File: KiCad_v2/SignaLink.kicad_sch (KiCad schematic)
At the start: 19 parts, among them U2 ESP32-C3_SUPERMINI_TH, U3 DM-OLED096-636, U7 LTC4415IMSE_PBF

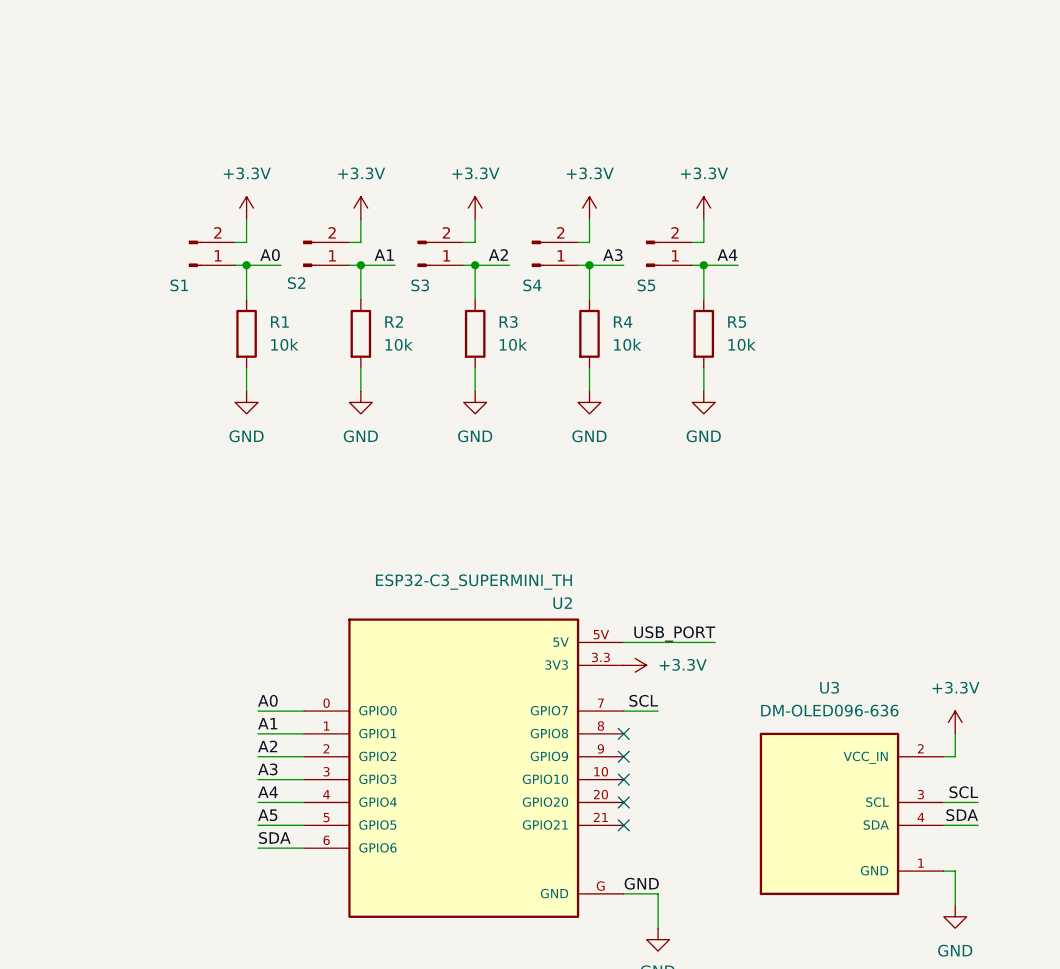
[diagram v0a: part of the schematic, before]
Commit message: feat: agrego 3d de ESP32 Y CM4
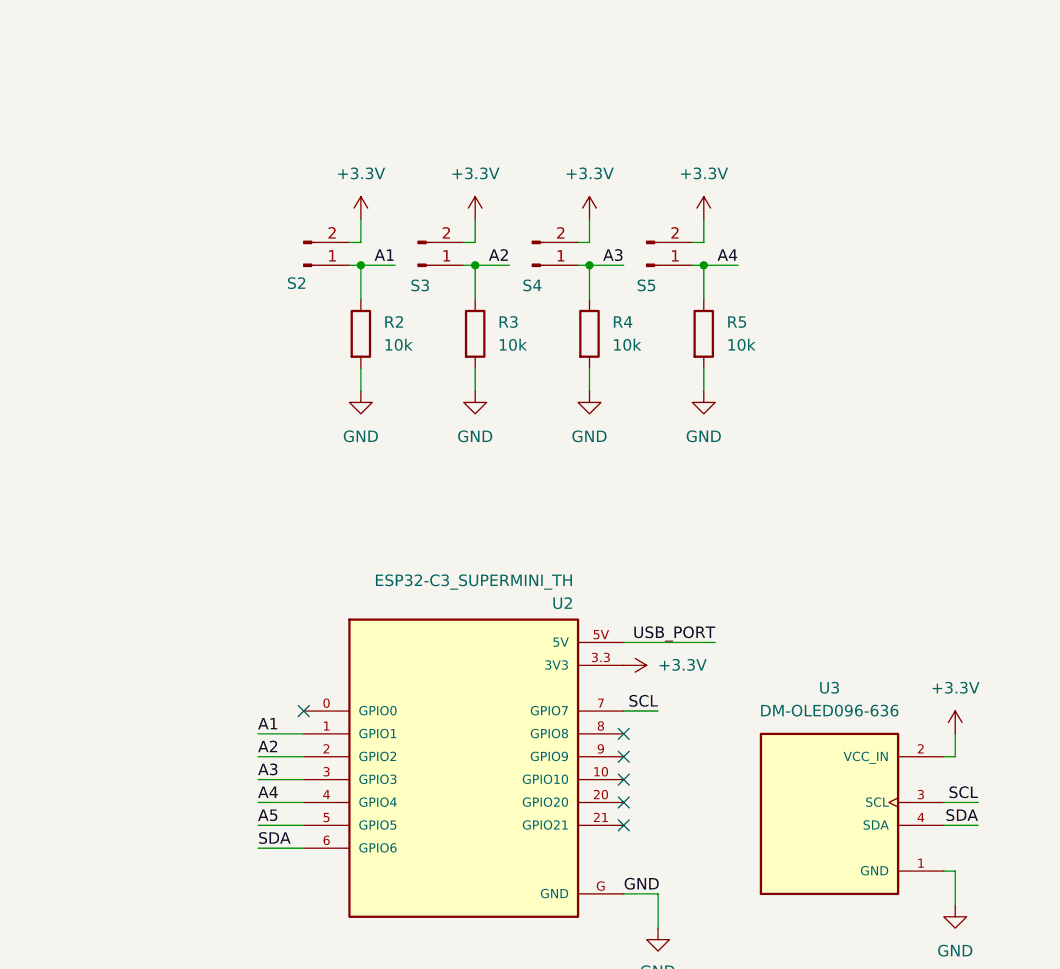
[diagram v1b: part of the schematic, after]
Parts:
- removed R1: 10k, Resistor_SMD:R_0805_2012Metric, symbol Device:R
- removed S1: SF 1, Connector_PinHeader_2.54mm:PinHeader_1x02_P2.54mm_Vertical, symbol Connector:Conn_01x02_Pin
- S2: footprint Connector_PinHeader_2.54mm:PinHeader_1x02_P2.54mm_Vertical -> Molex_KK-254_AE-6410-02A_1x02_P2.54mm_Vertical
- S3, S4: footprint Connector_PinHeader_2.54mm:PinHeader_1x02_P2.54mm_Vertical -> Connector_Molex:Molex_KK-254_AE-6410-02A_1x02_P2.54mm_Vertical
- U2: footprint esp32-huella:MODULE_ESP32-C3_SUPERMINI_TH -> Custom_Footprints:MODULE_ESP32-C3_SUPERMINI_TH
- U3: footprint Connector_PinHeader_2.54mm:PinHeader_1x04_P2.54mm_Vertical -> Custom_Footprints:MODULE_DM-OLED096-636
- U7: footprint Footprint KiCad:MSOP-16_MSE -> Custom_Footprints:MSOP-16_MSE
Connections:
- net A0: no longer names the net of U2.0 (GPIO0)
- no-connect marks 12 -> 13

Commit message: docs: muevo a carpetas los simbolos
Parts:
- S2: footprint Molex_KK-254_AE-6410-02A_1x02_P2.54mm_Vertical -> Connector_Molex:Molex_KK-254_AE-6410-02A_1x02_P2.54mm_Vertical
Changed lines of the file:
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@@
 			)
 		)
-		(property "Footprint" "Molex_KK-254_AE-6410-02A_1x02_P2.54mm_Vertical"
+		(property "Footprint" "Connector_Molex:Molex_KK-254_AE-6410-02A_1x02_P2.54mm_Vertical"
 			(at 52.07 38.1 0)
 			(effects

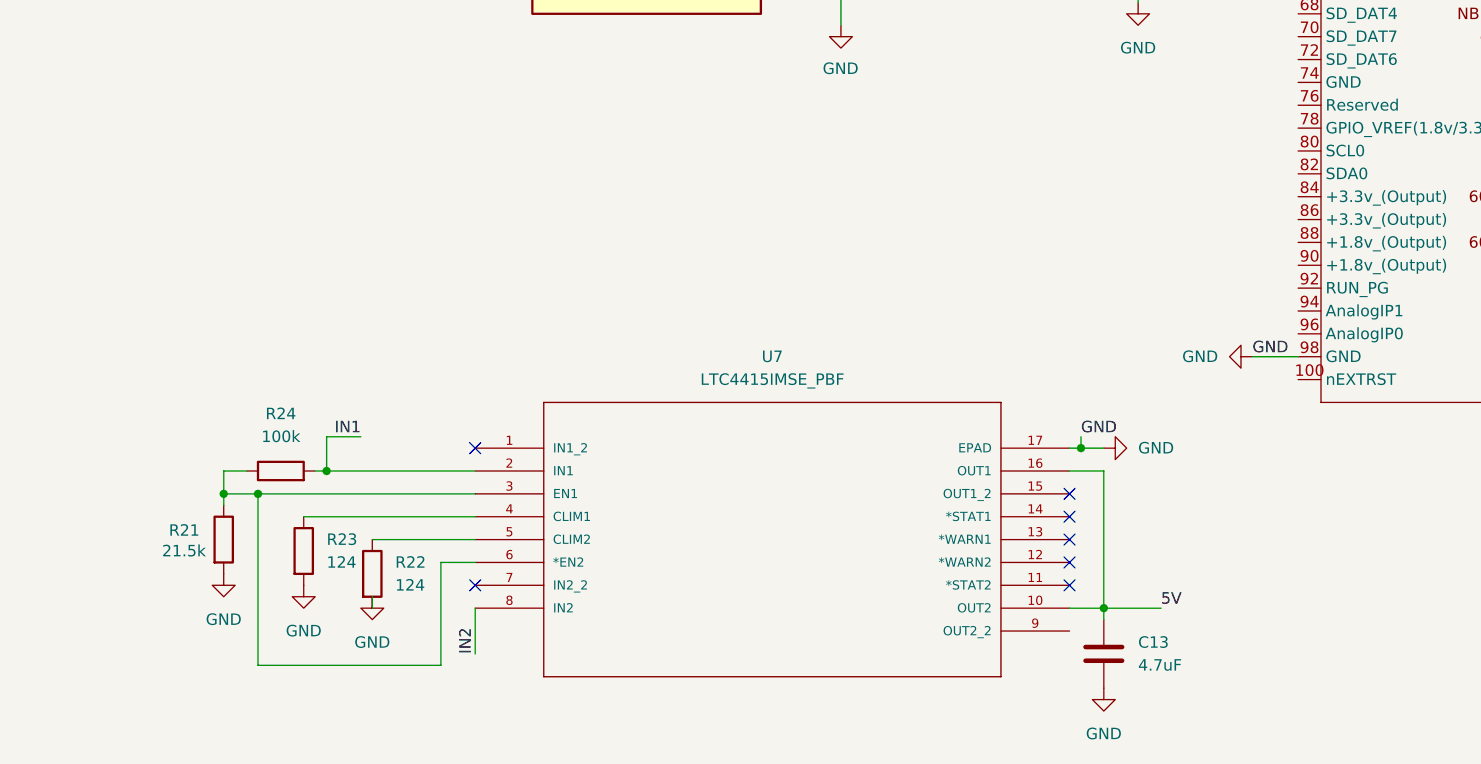
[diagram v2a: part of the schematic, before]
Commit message: agrego step up para 3A con su debido esquematico
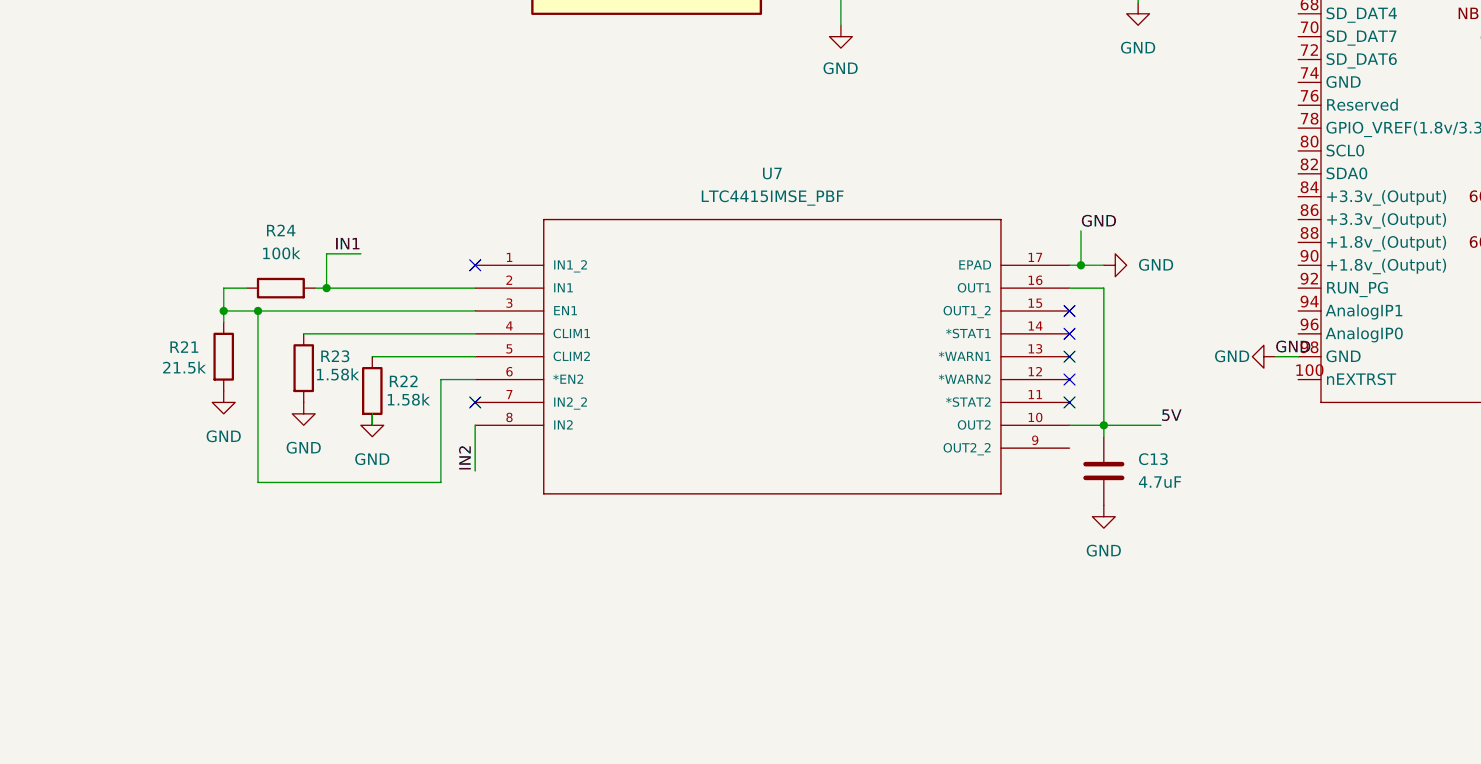
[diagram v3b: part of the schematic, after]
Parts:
- R22, R23: value 124 -> 1.58k
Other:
- moved on the sheet: C13, R21, R22, R23, R24, U7

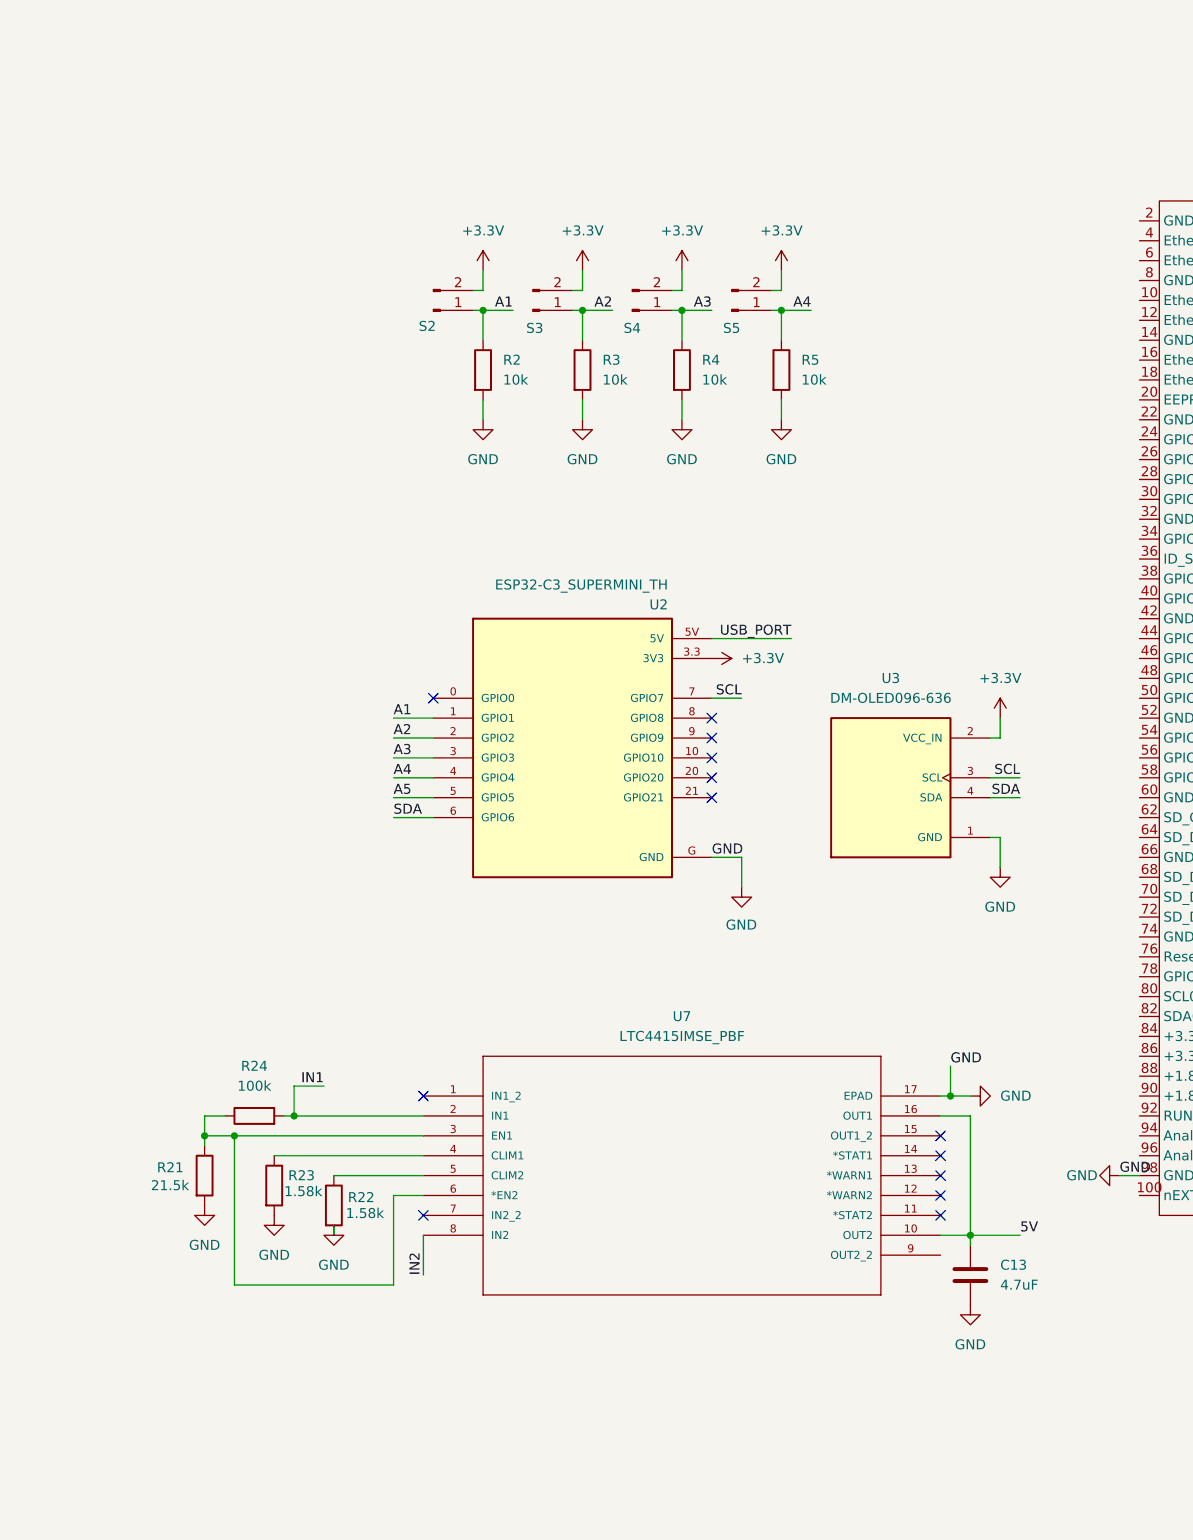
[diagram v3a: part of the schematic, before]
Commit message: agrego boton de wake
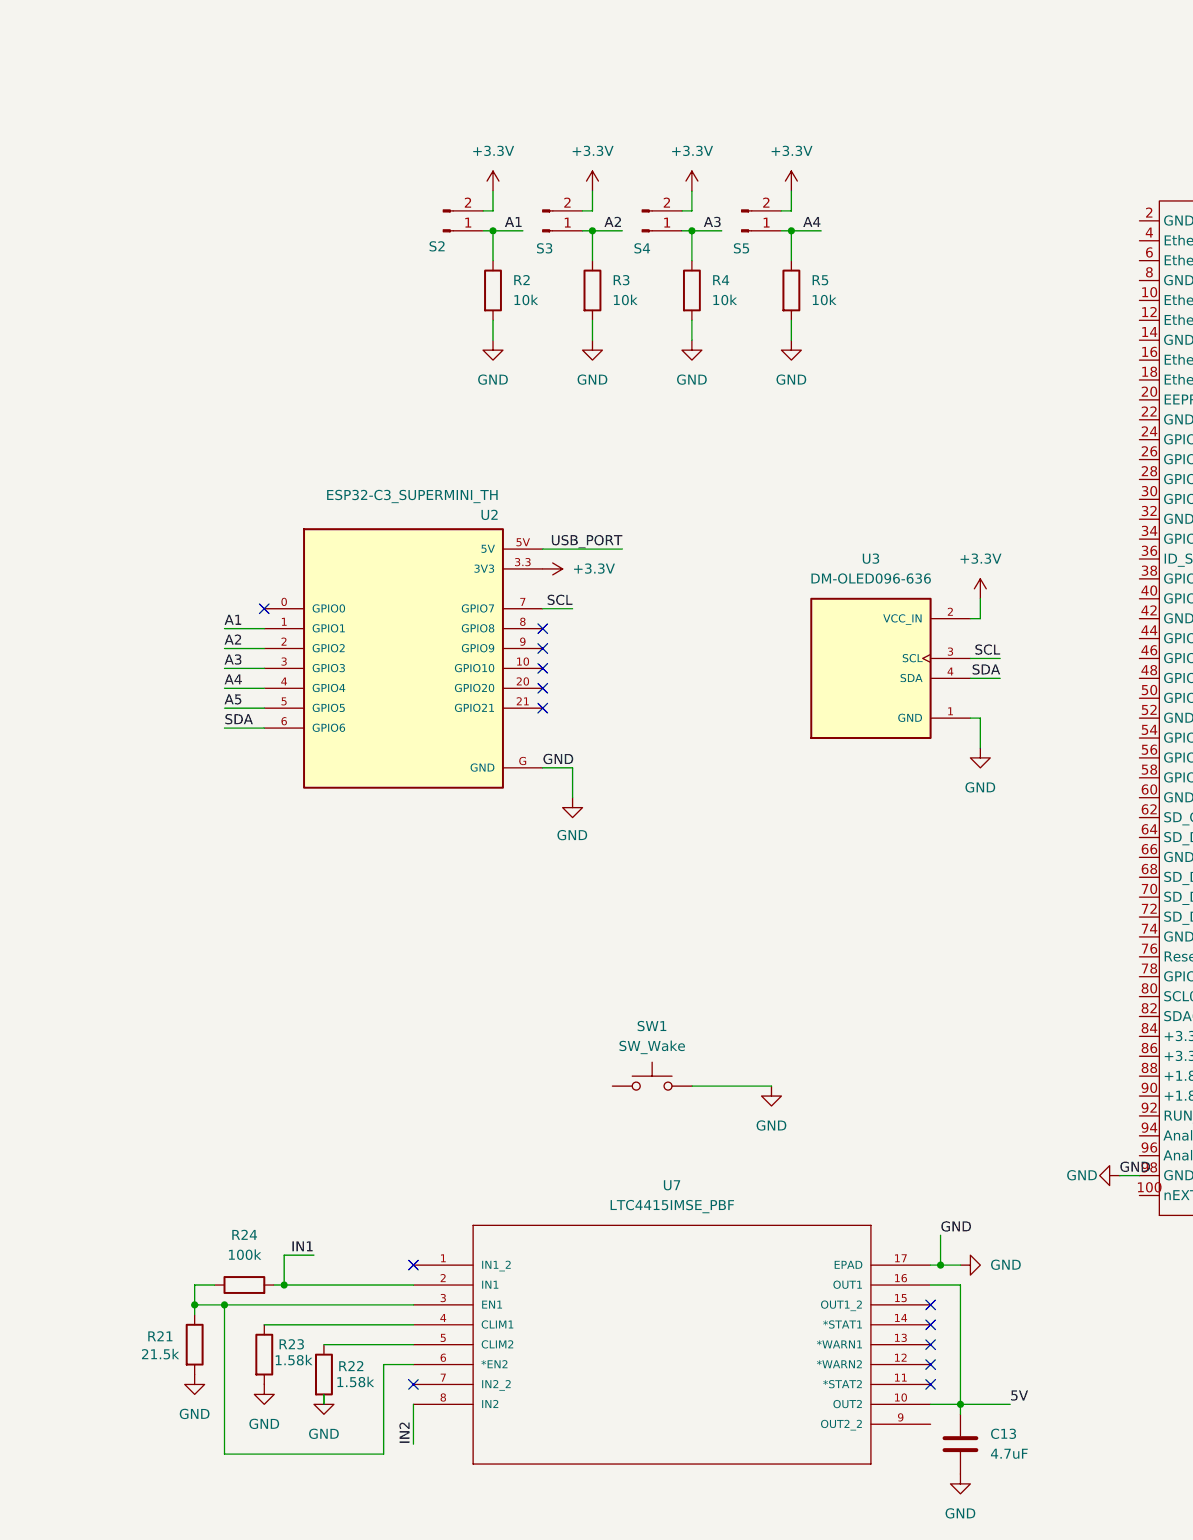
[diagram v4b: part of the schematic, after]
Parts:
- added SW1: SW_Wake, symbol Switch:SW_Push
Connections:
- net GND: now also SW1.2
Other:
- moved on the sheet: C13, R2, R21, R22, R23, R24, R3, R4, R5, S2, S3, S4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
